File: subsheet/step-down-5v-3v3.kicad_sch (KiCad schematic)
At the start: 7 parts, among them U901 TLV62569DBV

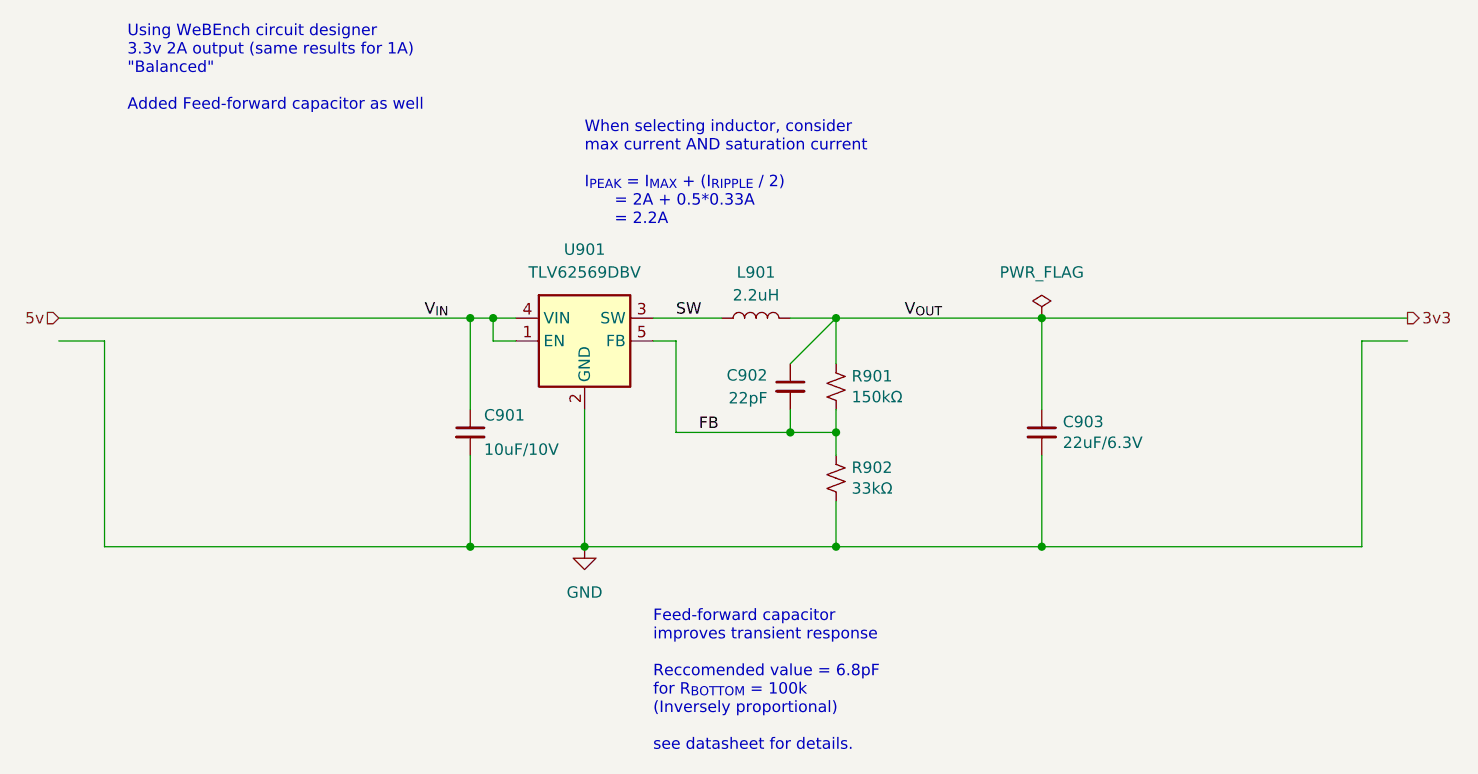
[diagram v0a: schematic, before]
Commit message: PCB changes, added useful connectors
Added a whole bunch of things that should make it useful - e.g.
ethernet, an extra flash chip for general storage, piicodev connectors
for I2C.

Also added a GPIB connector footprint; dev-board version worked nicely,
but may as well make this work for that too. Saves bying dev boards : )
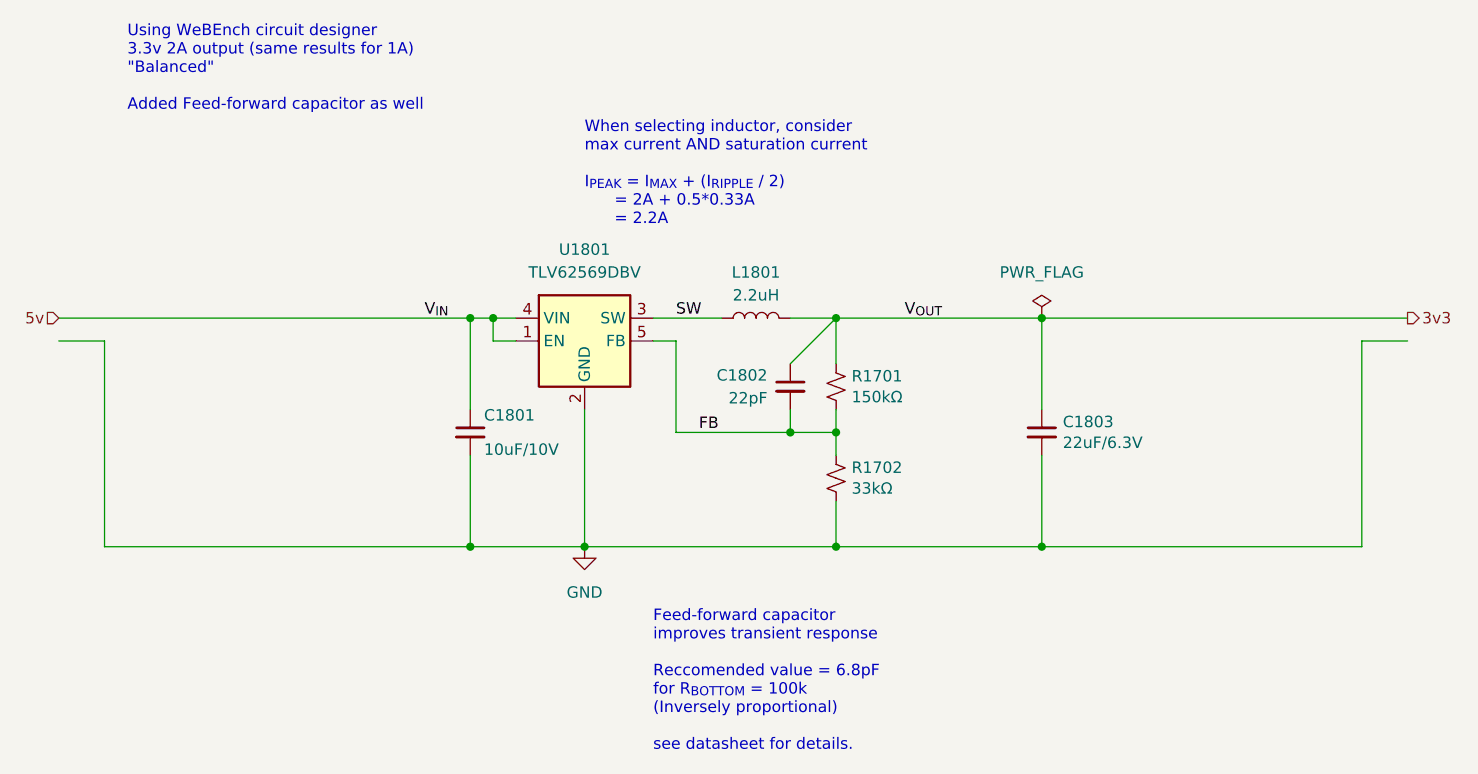
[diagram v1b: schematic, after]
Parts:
- renumbered C901 to C1801, C902 to C1802, C903 to C1803, L901 to L1801, R901 to R1701, R902 to R1702, U901 to U1801

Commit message: Uknown changes?File formats?
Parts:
- renumbered C1801 to C901, C1802 to C902, C1803 to C903, L1801 to L901, R1701 to R901, R1702 to R902, U1801 to U901
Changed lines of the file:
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@@
 		(on_board yes)
 		(dnp no)
-		(property "Reference" "C1803"
+		(property "Reference" "C903"
 			(at 136.9568 62.3316 0)
 			(effects
@@
 			(project "ESP_bare_chip_test_board"
 				(path "/45b6f84a-e69b-48be-a49b-bc68872e2c15/28425a28-8968-4679-b18b-58814452f93f/ed6f4ea4-2fc2-4f57-9b20-06c5785a7384"
-					(reference "C1803")
-					(unit 1)
-				)
-				(path "/45b6f84a-e69b-48be-a49b-bc68872e2c15/28425a28-8968-4679-b18b-58814452f93f/cab84238-ee51-476d-8b41-60559ed008d0"
-					(reference "C1803")
+					(reference "C903")
+					(unit 1)
+				)
+				(path "/45b6f84a-e69b-48be-a49b-bc68872e2c15/28425a28-8968-4679-b18b-58814452f93f/cab84238-ee51-476d-8b41-60559ed008d0"
+					(reference "C1003")
 					(unit 1)
 				)
@@
 		(dnp no)
 		(fields_autoplaced yes)
-		(property "Reference" "L1801"
+		(property "Reference" "L901"
 			(at 102.87 45.72 90)
 			(effects
@@
 			(project "ESP_bare_chip_test_board"
 				(path "/45b6f84a-e69b-48be-a49b-bc68872e2c15/28425a28-8968-4679-b18b-58814452f93f/ed6f4ea4-2fc2-4f57-9b20-06c5785a7384"
-					(reference "L1801")
-					(unit 1)
-				)
-				(path "/45b6f84a-e69b-48be-a49b-bc68872e2c15/28425a28-8968-4679-b18b-58814452f93f/cab84238-ee51-476d-8b41-60559ed008d0"
-					(reference "L1801")
+					(reference "L901")
+					(unit 1)
+				)
+				(path "/45b6f84a-e69b-48be-a49b-bc68872e2c15/28425a28-8968-4679-b18b-58814452f93f/cab84238-ee51-476d-8b41-60559ed008d0"
+					(reference "L1001")
 					(unit 1)
 				)
@@
 		(dnp no)
 		(fields_autoplaced yes)
-		(property "Reference" "C1802"
+		(property "Reference" "C902"
 			(at 104.14 57.1563 0)
 			(effects
@@
 			(project "ESP_bare_chip_test_board"
 				(path "/45b6f84a-e69b-48be-a49b-bc68872e2c15/28425a28-8968-4679-b18b-58814452f93f/ed6f4ea4-2fc2-4f57-9b20-06c5785a7384"
-					(reference "C1802")
-					(unit 1)
-				)
-				(path "/45b6f84a-e69b-48be-a49b-bc68872e2c15/28425a28-8968-4679-b18b-58814452f93f/cab84238-ee51-476d-8b41-60559ed008d0"
-					(reference "C1802")
+					(reference "C902")
+					(unit 1)
+				)
+				(path "/45b6f84a-e69b-48be-a49b-bc68872e2c15/28425a28-8968-4679-b18b-58814452f93f/cab84238-ee51-476d-8b41-60559ed008d0"
+					(reference "C1002")
 					(unit 1)
 				)
@@
 		(on_board yes)
 		(dnp no)
-		(property "Reference" "R1701"
+		(property "Reference" "R901"
 			(at 113.4872 57.2516 0)
 			(effects
@@
 			(project "ESP_bare_chip_test_board"
 				(path "/45b6f84a-e69b-48be-a49b-bc68872e2c15/28425a28-8968-4679-b18b-58814452f93f/ed6f4ea4-2fc2-4f57-9b20-06c5785a7384"
-					(reference "R1701")
-					(unit 1)
-				)
-				(path "/45b6f84a-e69b-48be-a49b-bc68872e2c15/28425a28-8968-4679-b18b-58814452f93f/cab84238-ee51-476d-8b41-60559ed008d0"
-					(reference "R1701")
+					(reference "R901")
+					(unit 1)
+				)
+				(path "/45b6f84a-e69b-48be-a49b-bc68872e2c15/28425a28-8968-4679-b18b-58814452f93f/cab84238-ee51-476d-8b41-60559ed008d0"
+					(reference "R1001")
 					(unit 1)
 				)
@@
 		(dnp no)
 		(fields_autoplaced yes)
-		(property "Reference" "U1801"
+		(property "Reference" "U901"
 			(at 83.82 43.18 0)
 			(effects
@@
 			(project "ESP_bare_chip_test_board"
 				(path "/45b6f84a-e69b-48be-a49b-bc68872e2c15/28425a28-8968-4679-b18b-58814452f93f/ed6f4ea4-2fc2-4f57-9b20-06c5785a7384"
-					(reference "U1801")
-					(unit 1)
-				)
-				(path "/45b6f84a-e69b-48be-a49b-bc68872e2c15/28425a28-8968-4679-b18b-58814452f93f/cab84238-ee51-476d-8b41-60559ed008d0"
-					(reference "U1801")
+					(reference "U901")
+					(unit 1)
+				)
+				(path "/45b6f84a-e69b-48be-a49b-bc68872e2c15/28425a28-8968-4679-b18b-58814452f93f/cab84238-ee51-476d-8b41-60559ed008d0"
+					(reference "U1001")
 					(unit 1)
 				)
@@
 		(dnp no)
 		(fields_autoplaced yes)
-		(property "Reference" "#FLG01701"
+		(property "Reference" "#FLG0901"
 			(at 134.62 48.895 0)
 			(effects
@@
 			(project "ESP_bare_chip_test_board"
 				(path "/45b6f84a-e69b-48be-a49b-bc68872e2c15/28425a28-8968-4679-b18b-58814452f93f/ed6f4ea4-2fc2-4f57-9b20-06c5785a7384"
-					(reference "#FLG01701")
-					(unit 1)
-				)
-				(path "/45b6f84a-e69b-48be-a49b-bc68872e2c15/28425a28-8968-4679-b18b-58814452f93f/cab84238-ee51-476d-8b41-60559ed008d0"
-					(reference "#FLG01701")
+					(reference "#FLG0901")
+					(unit 1)
+				)
+				(path "/45b6f84a-e69b-48be-a49b-bc68872e2c15/28425a28-8968-4679-b18b-58814452f93f/cab84238-ee51-476d-8b41-60559ed008d0"
+					(reference "#FLG01001")
 					(unit 1)
 				)
@@
 		(dnp no)
 		(fields_autoplaced yes)
-		(property "Reference" "#PWR01801"
+		(property "Reference" "#PWR0901"
 			(at 83.82 82.55 0)
 			(effects
@@
 			(project "ESP_bare_chip_test_board"
 				(path "/45b6f84a-e69b-48be-a49b-bc68872e2c15/28425a28-8968-4679-b18b-58814452f93f/ed6f4ea4-2fc2-4f57-9b20-06c5785a7384"
-					(reference "#PWR01801")
-					(unit 1)
-				)
-				(path "/45b6f84a-e69b-48be-a49b-bc68872e2c15/28425a28-8968-4679-b18b-58814452f93f/cab84238-ee51-476d-8b41-60559ed008d0"
-					(reference "#PWR01801")
+					(reference "#PWR0901")
+					(unit 1)
+				)
+				(path "/45b6f84a-e69b-48be-a49b-bc68872e2c15/28425a28-8968-4679-b18b-58814452f93f/cab84238-ee51-476d-8b41-60559ed008d0"
+					(reference "#PWR01001")
 					(unit 1)
 				)
@@
 		(on_board yes)
 		(dnp no)
-		(property "Reference" "R1702"
+		(property "Reference" "R902"
 			(at 113.4872 67.4116 0)
 			(effects
@@
 			(project "ESP_bare_chip_test_board"
 				(path "/45b6f84a-e69b-48be-a49b-bc68872e2c15/28425a28-8968-4679-b18b-58814452f93f/ed6f4ea4-2fc2-4f57-9b20-06c5785a7384"
-					(reference "R1702")
-					(unit 1)
-				)
-				(path "/45b6f84a-e69b-48be-a49b-bc68872e2c15/28425a28-8968-4679-b18b-58814452f93f/cab84238-ee51-476d-8b41-60559ed008d0"
-					(reference "R1702")
+					(reference "R902")
+					(unit 1)
+				)
+				(path "/45b6f84a-e69b-48be-a49b-bc68872e2c15/28425a28-8968-4679-b18b-58814452f93f/cab84238-ee51-476d-8b41-60559ed008d0"
+					(reference "R1002")
 					(unit 1)
 				)
@@
 		(on_board yes)
 		(dnp no)
-		(property "Reference" "C1801"
+		(property "Reference" "C901"
 			(at 72.644 61.595 0)
 			(effects
@@
 			(project "ESP_bare_chip_test_board"
 				(path "/45b6f84a-e69b-48be-a49b-bc68872e2c15/28425a28-8968-4679-b18b-58814452f93f/ed6f4ea4-2fc2-4f57-9b20-06c5785a7384"
-					(reference "C1801")
-					(unit 1)
-				)
-				(path "/45b6f84a-e69b-48be-a49b-bc68872e2c15/28425a28-8968-4679-b18b-58814452f93f/cab84238-ee51-476d-8b41-60559ed008d0"
-					(reference "C1801")
-					(unit 1)
-				)
+					(reference "C901")
+					(unit 1)
+				)
+				(path "/45b6f84a-e69b-48be-a49b-bc68872e2c15/28425a28-8968-4679-b18b-58814452f93f/cab84238-ee51-476d-8b41-60559ed008d0"
+					(reference "C1001")
+					(unit 1)
+				)

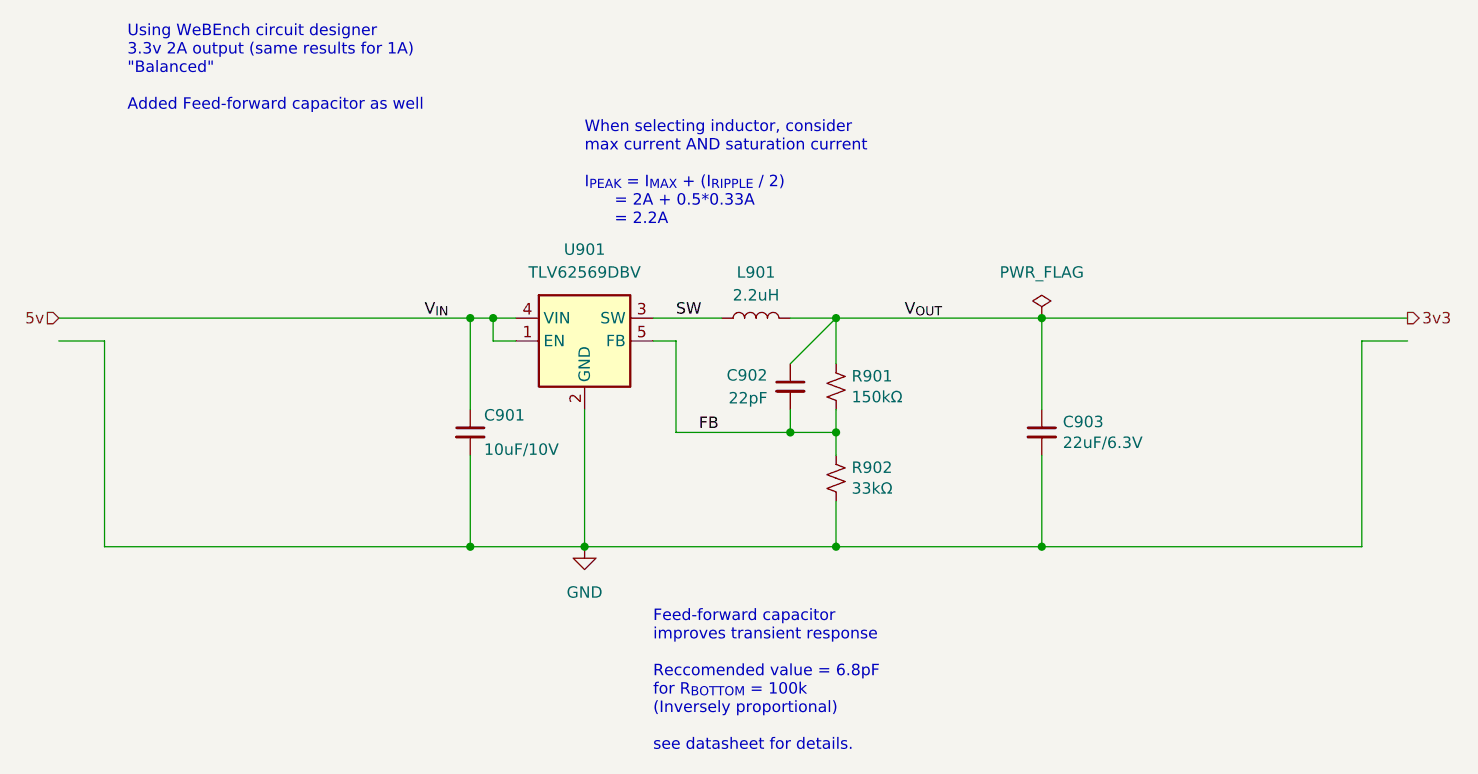
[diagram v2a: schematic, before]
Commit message: Unknown changes? Arranging components, I believe
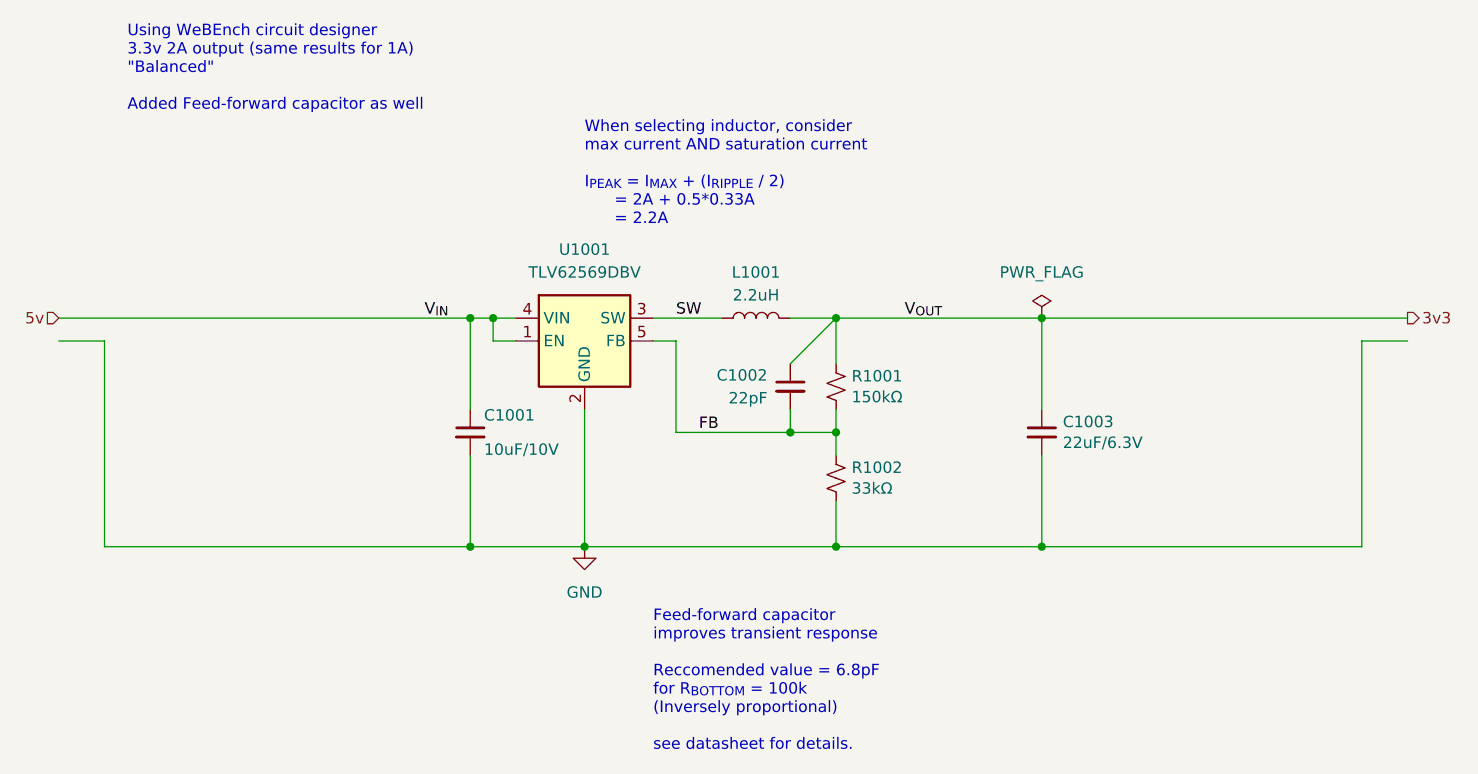
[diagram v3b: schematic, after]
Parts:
- renumbered C901 to C1001, C902 to C1002, C903 to C1003, L901 to L1001, R901 to R1001, R902 to R1002, U901 to U1001
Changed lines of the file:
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@@
 		(on_board yes)
 		(dnp no)
-		(property "Reference" "C903"
+		(property "Reference" "C1003"
 			(at 136.9568 62.3316 0)
 			(effects
@@
 		(instances
 			(project "ESP_bare_chip_test_board"
-				(path "/45b6f84a-e69b-48be-a49b-bc68872e2c15/28425a28-8968-4679-b18b-58814452f93f/ed6f4ea4-2fc2-4f57-9b20-06c5785a7384"
-					(reference "C903")
-					(unit 1)
-				)
 				(path "/45b6f84a-e69b-48be-a49b-bc68872e2c15/28425a28-8968-4679-b18b-58814452f93f/cab84238-ee51-476d-8b41-60559ed008d0"
 					(reference "C1003")
@@
 		(dnp no)
 		(fields_autoplaced yes)
-		(property "Reference" "L901"
+		(property "Reference" "L1001"
 			(at 102.87 45.72 90)
 			(effects
@@
 		(instances
 			(project "ESP_bare_chip_test_board"
-				(path "/45b6f84a-e69b-48be-a49b-bc68872e2c15/28425a28-8968-4679-b18b-58814452f93f/ed6f4ea4-2fc2-4f57-9b20-06c5785a7384"
-					(reference "L901")
-					(unit 1)
-				)
 				(path "/45b6f84a-e69b-48be-a49b-bc68872e2c15/28425a28-8968-4679-b18b-58814452f93f/cab84238-ee51-476d-8b41-60559ed008d0"
 					(reference "L1001")
@@
 		(dnp no)
 		(fields_autoplaced yes)
-		(property "Reference" "C902"
+		(property "Reference" "C1002"
 			(at 104.14 57.1563 0)
 			(effects
@@
 		(instances
 			(project "ESP_bare_chip_test_board"
-				(path "/45b6f84a-e69b-48be-a49b-bc68872e2c15/28425a28-8968-4679-b18b-58814452f93f/ed6f4ea4-2fc2-4f57-9b20-06c5785a7384"
-					(reference "C902")
-					(unit 1)
-				)
 				(path "/45b6f84a-e69b-48be-a49b-bc68872e2c15/28425a28-8968-4679-b18b-58814452f93f/cab84238-ee51-476d-8b41-60559ed008d0"
 					(reference "C1002")
@@
 		(on_board yes)
 		(dnp no)
-		(property "Reference" "R901"
+		(property "Reference" "R1001"
 			(at 113.4872 57.2516 0)
 			(effects
@@
 		(instances
 			(project "ESP_bare_chip_test_board"
-				(path "/45b6f84a-e69b-48be-a49b-bc68872e2c15/28425a28-8968-4679-b18b-58814452f93f/ed6f4ea4-2fc2-4f57-9b20-06c5785a7384"
-					(reference "R901")
-					(unit 1)
-				)
 				(path "/45b6f84a-e69b-48be-a49b-bc68872e2c15/28425a28-8968-4679-b18b-58814452f93f/cab84238-ee51-476d-8b41-60559ed008d0"
 					(reference "R1001")
@@
 		(dnp no)
 		(fields_autoplaced yes)
-		(property "Reference" "U901"
+		(property "Reference" "U1001"
 			(at 83.82 43.18 0)
 			(effects
@@
 		(instances
 			(project "ESP_bare_chip_test_board"
-				(path "/45b6f84a-e69b-48be-a49b-bc68872e2c15/28425a28-8968-4679-b18b-58814452f93f/ed6f4ea4-2fc2-4f57-9b20-06c5785a7384"
-					(reference "U901")
-					(unit 1)
-				)
 				(path "/45b6f84a-e69b-48be-a49b-bc68872e2c15/28425a28-8968-4679-b18b-58814452f93f/cab84238-ee51-476d-8b41-60559ed008d0"
 					(reference "U1001")
@@
 		(dnp no)
 		(fields_autoplaced yes)
-		(property "Reference" "#FLG0901"
+		(property "Reference" "#FLG01001"
 			(at 134.62 48.895 0)
 			(effects
@@
 		(instances
 			(project "ESP_bare_chip_test_board"
-				(path "/45b6f84a-e69b-48be-a49b-bc68872e2c15/28425a28-8968-4679-b18b-58814452f93f/ed6f4ea4-2fc2-4f57-9b20-06c5785a7384"
-					(reference "#FLG0901")
-					(unit 1)
-				)
 				(path "/45b6f84a-e69b-48be-a49b-bc68872e2c15/28425a28-8968-4679-b18b-58814452f93f/cab84238-ee51-476d-8b41-60559ed008d0"
 					(reference "#FLG01001")
@@
 		(dnp no)
 		(fields_autoplaced yes)
-		(property "Reference" "#PWR0901"
+		(property "Reference" "#PWR01001"
 			(at 83.82 82.55 0)
 			(effects
@@
 		(instances
 			(project "ESP_bare_chip_test_board"
-				(path "/45b6f84a-e69b-48be-a49b-bc68872e2c15/28425a28-8968-4679-b18b-58814452f93f/ed6f4ea4-2fc2-4f57-9b20-06c5785a7384"
-					(reference "#PWR0901")
-					(unit 1)
-				)
 				(path "/45b6f84a-e69b-48be-a49b-bc68872e2c15/28425a28-8968-4679-b18b-58814452f93f/cab84238-ee51-476d-8b41-60559ed008d0"
 					(reference "#PWR01001")
@@
 		(on_board yes)
 		(dnp no)
-		(property "Reference" "R902"
+		(property "Reference" "R1002"
 			(at 113.4872 67.4116 0)
 			(effects
@@
 		(instances
 			(project "ESP_bare_chip_test_board"
-				(path "/45b6f84a-e69b-48be-a49b-bc68872e2c15/28425a28-8968-4679-b18b-58814452f93f/ed6f4ea4-2fc2-4f57-9b20-06c5785a7384"
-					(reference "R902")
-					(unit 1)
-				)
 				(path "/45b6f84a-e69b-48be-a49b-bc68872e2c15/28425a28-8968-4679-b18b-58814452f93f/cab84238-ee51-476d-8b41-60559ed008d0"
 					(reference "R1002")
@@
 		(on_board yes)
 		(dnp no)
-		(property "Reference" "C901"
+		(property "Reference" "C1001"
 			(at 72.644 61.595 0)
 			(effects
@@
 		(instances
 			(project "ESP_bare_chip_test_board"
-				(path "/45b6f84a-e69b-48be-a49b-bc68872e2c15/28425a28-8968-4679-b18b-58814452f93f/ed6f4ea4-2fc2-4f57-9b20-06c5785a7384"
-					(reference "C901")
-					(unit 1)
-				)
 				(path "/45b6f84a-e69b-48be-a49b-bc68872e2c15/28425a28-8968-4679-b18b-58814452f93f/cab84238-ee51-476d-8b41-60559ed008d0"
 					(reference "C1001")

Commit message: Add JLCPCB corrections for new components
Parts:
- U1001: JLCPCB_CORRECTION 0;0;180 -> 0;0;90
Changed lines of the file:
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@@
 			)
 		)
-		(property "JLCPCB_CORRECTION" "0;0;180"
+		(property "JLCPCB_CORRECTION" "0;0;90"
 			(at 83.82 53.34 0)
 			(effects

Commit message: Silkscreen work. Edit tittle block/version number
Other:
- company: copyright Escape This 2024 -> (c) Vincent Dalstra
- title: Puzzle Board -> Untitled 4-layer JLCPCB
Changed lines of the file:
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@@
 	(paper "A5")
 	(title_block
-		(title "Puzzle Board")
-		(date "2024-03-20")
-		(rev "4.0.0")
-		(company "copyright Escape This 2024")
+		(title "Untitled 4-layer JLCPCB")
+		(date "2024-06-14")
+		(rev "1.0.0")
+		(company "(c) Vincent Dalstra")
 		(comment 1 "Drawn by: VGD")
 		(comment 2 "Check by:")

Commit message: Final corrections and silkscreen labels
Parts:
- U1001: JLCPCB_CORRECTION 0;0;90 -> 0;0;180
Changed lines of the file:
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@@
 			)
 		)
-		(property "JLCPCB_CORRECTION" "0;0;90"
+		(property "JLCPCB_CORRECTION" "0;0;180"
 			(at 83.82 53.34 0)
 			(effects
